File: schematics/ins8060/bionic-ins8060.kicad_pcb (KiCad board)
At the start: 2 copper layers, 25.4 x 68.6 mm, 8 parts, among them J1 Bionic-P135, J2 Bionic-P245, U1 INS8060, U2 11AA010-I/TT

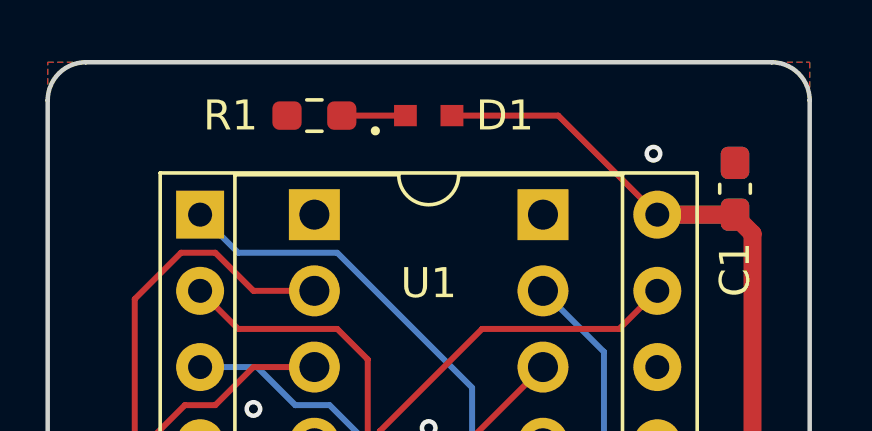
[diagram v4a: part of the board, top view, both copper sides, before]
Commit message: [schematics] Update LED footprint
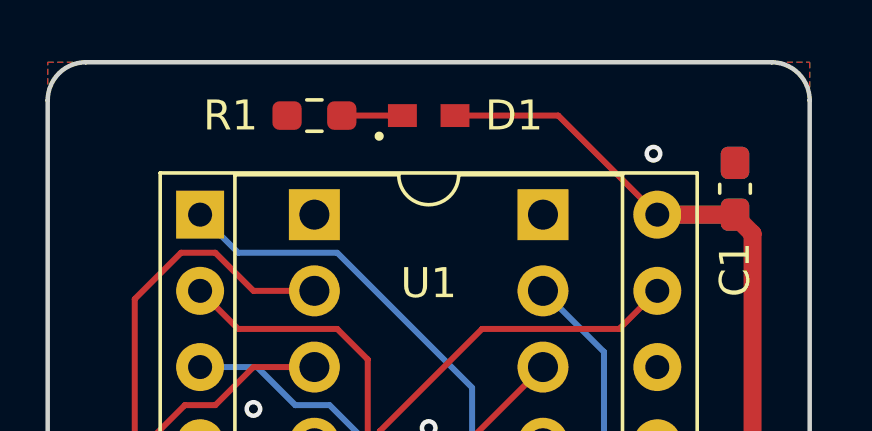
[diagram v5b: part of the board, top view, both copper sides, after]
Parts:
- D1: footprint 0-LocalLibrary:LED_CSL1901UW1_ROM -> 0-LocalLibrary:LED_CSL1901UW1_ROM-M

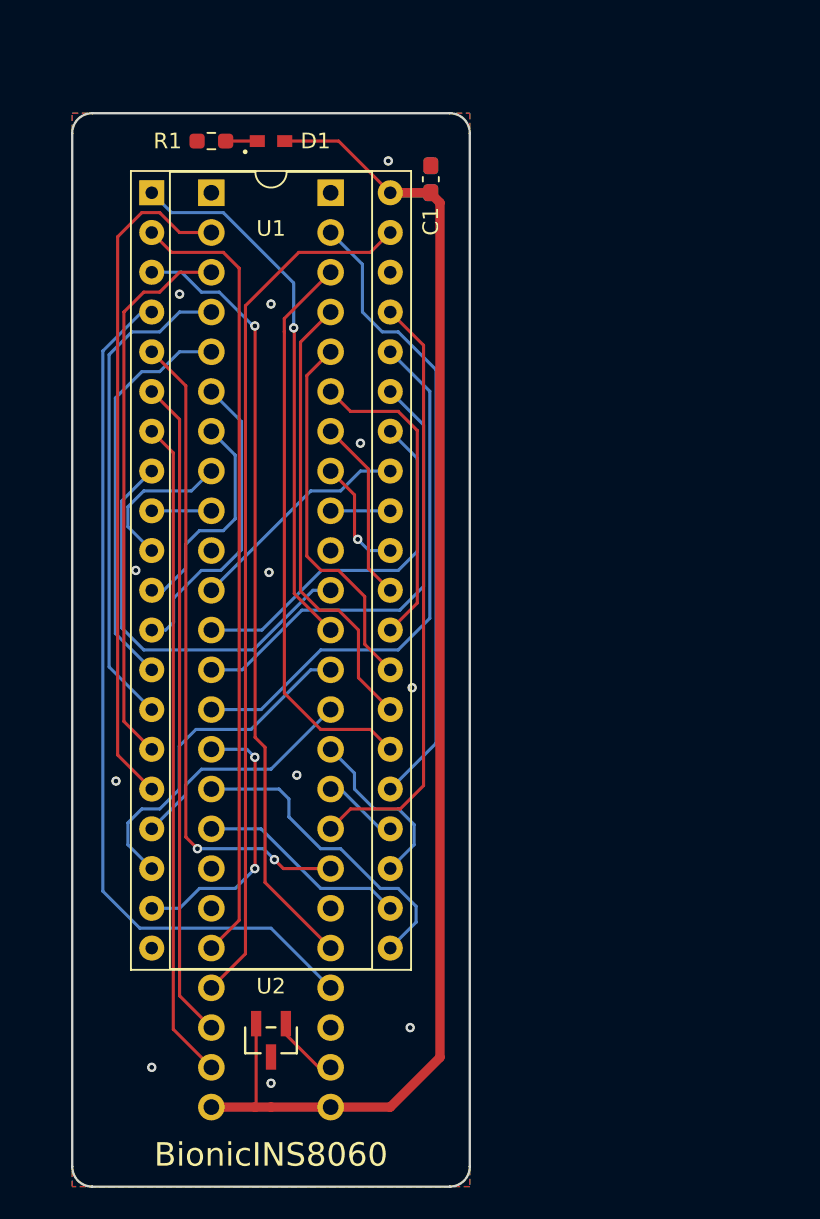
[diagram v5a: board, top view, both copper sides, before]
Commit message: [INS8060] Cleanup schematics
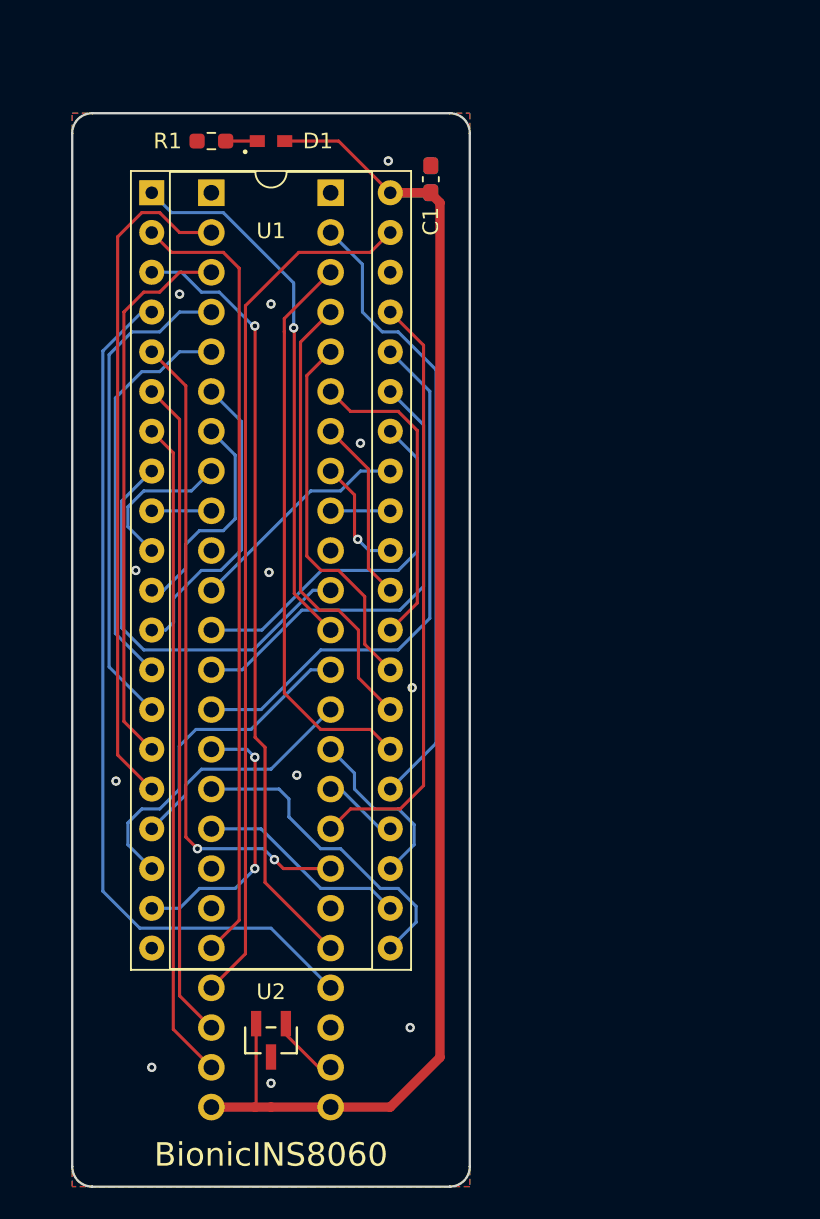
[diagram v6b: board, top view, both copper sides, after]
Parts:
- D1: footprint 0-LocalLibrary:LED_CSL1901UW1_ROM-M -> rhom:LED_CSL1901UW1_ROM-M
- J1: footprint 0-LocalLibrary:Bionic-P135_Vertical -> bionic:Bionic-P135_Vertical
- J2: footprint 0-LocalLibrary:Bionic-P245_Vertical -> bionic:Bionic-P245_Vertical
- U1: footprint 0-LocalLibrary:DIP-40_W15.24mm_Socket -> bionic:DIP-40_W15.24mm_Socket
- U2: footprint 0-LocalLibrary:SOT-23_MC_MCH-M -> microchip:SOT-23_MC_MCH-M
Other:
- rule pad_to_mask_clearance: 0.051 -> 0
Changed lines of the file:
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@@
 	)
 	(setup
-		(pad_to_mask_clearance 0.051)
-		(solder_mask_min_width 0.25)
+		(pad_to_mask_clearance 0)
 		(allow_soldermask_bridges_in_footprints no)
 		(aux_axis_origin 101 70)
@@
 	(net 47 "unconnected-(U1-XOUT-Pad38)")
 	(net 48 "Net-(D1-K)")
-	(footprint "0-LocalLibrary:LED_CSL1901UW1_ROM-M"
+	(footprint "rhom:LED_CSL1901UW1_ROM-M"
 		(layer "F.Cu")
 		(at 113.7 71.778)
@@
 		(tags "CSL1901UW1 ")
 		(property "Reference" "D1"
-			(at 2.8448 0 0)
+			(at 2.9972 0 0)
 			(unlocked yes)
 			(layer "F.SilkS")
@@
 			)
 		)
-		(property "Footprint" "0-LocalLibrary:LED_CSL1901UW1_ROM-M"
+		(property "Footprint" "rhom:LED_CSL1901UW1_ROM-M"
 			(at 0 0 0)
 			(layer "F.Fab")
@@
 			)
 		)
-		(property "Description" ""
+		(property "Description" "Red LED (Low Current Emission, SMD)"
 			(at 0 0 0)
 			(layer "F.Fab")
@@
 					(xy 113.3571 71.4224) (xy 114.0429 71.4224) (xy 114.0429 72.1336) (xy 113.3571 72.1336)
 				)
+			)
+		)
+		(model "${KIPRJMOD}/rhom.pretty/LED_CSL1901UW1_ROM.step"
+			(offset
+				(xyz 0 0 0)
+			)
+			(scale
+				(xyz 1 1 1)
+			)
+			(rotate
+				(xyz 0 0 0)
 			)
 		)
@@
 		)
 	)
-	(footprint "0-LocalLibrary:DIP-40_W15.24mm_Socket"
+	(footprint "bionic:DIP-40_W15.24mm_Socket"
 		(locked yes)
 		(layer "F.Cu")
@@
 		(tags "THT DIP DIL PDIP 2.54mm 15.24mm 600mil Socket")
 		(property "Reference" "U1"
-			(at 7.62 2.286 0)
+			(at 7.62 2.4384 0)
 			(layer "F.SilkS")
 			(effects
@@
 			)
 		)
-		(property "Footprint" "0-LocalLibrary:DIP-40_W15.24mm_Socket"
+		(property "Footprint" "bionic:DIP-40_W15.24mm_Socket"
 			(at 0 0 0)
 			(layer "F.Fab")
@@
 			)
 		)
-		(property "Description" ""
+		(property "Description" "8-bit General Purpose Microprocessor, DIP-40"
 			(at 0 0 0)
 			(layer "F.Fab")
@@
 		)
 	)
-	(footprint "0-LocalLibrary:SOT-23_MC_MCH-M"
+	(footprint "microchip:SOT-23_MC_MCH-M"
 		(layer "F.Cu")
 		(at 113.7 129.232 180)
 		(descr "Microchip 11AAxxx-I/TT UNI/O 1Kbit Serial EEPROM")
 		(property "Reference" "U2"
-			(at 0 3.4544 0)
+			(at 0 3.098 0)
 			(unlocked yes)
 			(layer "F.SilkS")
@@
 			)
 		)
-		(property "Footprint" "0-LocalLibrary:SOT-23_MC_MCH-M"
+		(property "Footprint" "microchip:SOT-23_MC_MCH-M"
 			(at 0 0 180)
 			(layer "F.Fab")
@@
 			)
 		)
-		(property "Description" ""
+		(property "Description" "UNI/O Serial EEPROM (1Kbit)"
 			(at 0 0 180)
 			(layer "F.Fab")
@@
 			(pintype "power_in")
 		)
-		(model "${KIPRJMOD}/0-LocalLibrary/SOT-23_MC_MCH.step"
+		(model "${KIPRJMOD}/microchip.pretty/SOT-23_MC_MCH.step"
 			(offset
 				(xyz 0 0 0)
@@
 		)
 	)
-	(footprint "0-LocalLibrary:Bionic-P245_Vertical"
+	(footprint "bionic:Bionic-P245_Vertical"
 		(locked yes)
 		(layer "B.Cu")
@@
 			)
 		)
-		(property "Footprint" "0-LocalLibrary:Bionic-P245_Vertical"
-			(at 0 0 180)
-			(layer "F.Fab")
+		(property "Footprint" "bionic:Bionic-P245_Vertical"
+			(at 0 0 0)
+			(layer "B.Fab")
 			(hide yes)
 			(effects
@@
 					(thickness 0.15)
 				)
+				(justify mirror)
 			)
 		)
 		(property "Datasheet" ""
-			(at 0 0 180)
-			(layer "F.Fab")
+			(at 0 0 0)
+			(layer "B.Fab")
 			(hide yes)
 			(effects
@@
 					(thickness 0.15)
 				)
-			)
-		)
-		(property "Description" ""
-			(at 0 0 180)
-			(layer "F.Fab")
+				(justify mirror)
+			)
+		)
+		(property "Description" "Generic connector, single row, 01x24, script generated (kicad-library-utils/schlib/autogen/connector/)"
+			(at 0 0 0)
+			(layer "B.Fab")
 			(hide yes)
 			(effects
@@
 					(thickness 0.15)
 				)
+				(justify mirror)
 			)
 		)
@@
 		)
 	)
-	(footprint "0-LocalLibrary:Bionic-P135_Vertical"
+	(footprint "bionic:Bionic-P135_Vertical"
 		(locked yes)
 		(layer "B.Cu")
@@
 			)
 		)
-		(property "Footprint" "0-LocalLibrary:Bionic-P135_Vertical"
-			(at 0 0 180)
-			(layer "F.Fab")
+		(property "Footprint" "bionic:Bionic-P135_Vertical"
+			(at 0 0 0)
+			(layer "B.Fab")
 			(hide yes)
 			(effects
@@
 					(thickness 0.15)
 				)
+				(justify mirror)
 			)
 		)
 		(property "Datasheet" ""
-			(at 0 0 180)
-			(layer "F.Fab")
+			(at 0 0 0)
+			(layer "B.Fab")
 			(hide yes)
 			(effects
@@
 					(thickness 0.15)
 				)
-			)
-		)
-		(property "Description" ""
-			(at 0 0 180)
-			(layer "F.Fab")
+				(justify mirror)
+			)
+		)
+		(property "Description" "Generic connector, single row, 01x24, script generated (kicad-library-utils/schlib/autogen/connector/)"
+			(at 0 0 0)
+			(layer "B.Fab")
 			(hide yes)
 			(effects
@@
 					(thickness 0.15)
 				)
-			)
-		)
+				(justify mirror)
+			)
+		)

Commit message: [INS8060] Update schematics
Remove unused pins from bionic connector
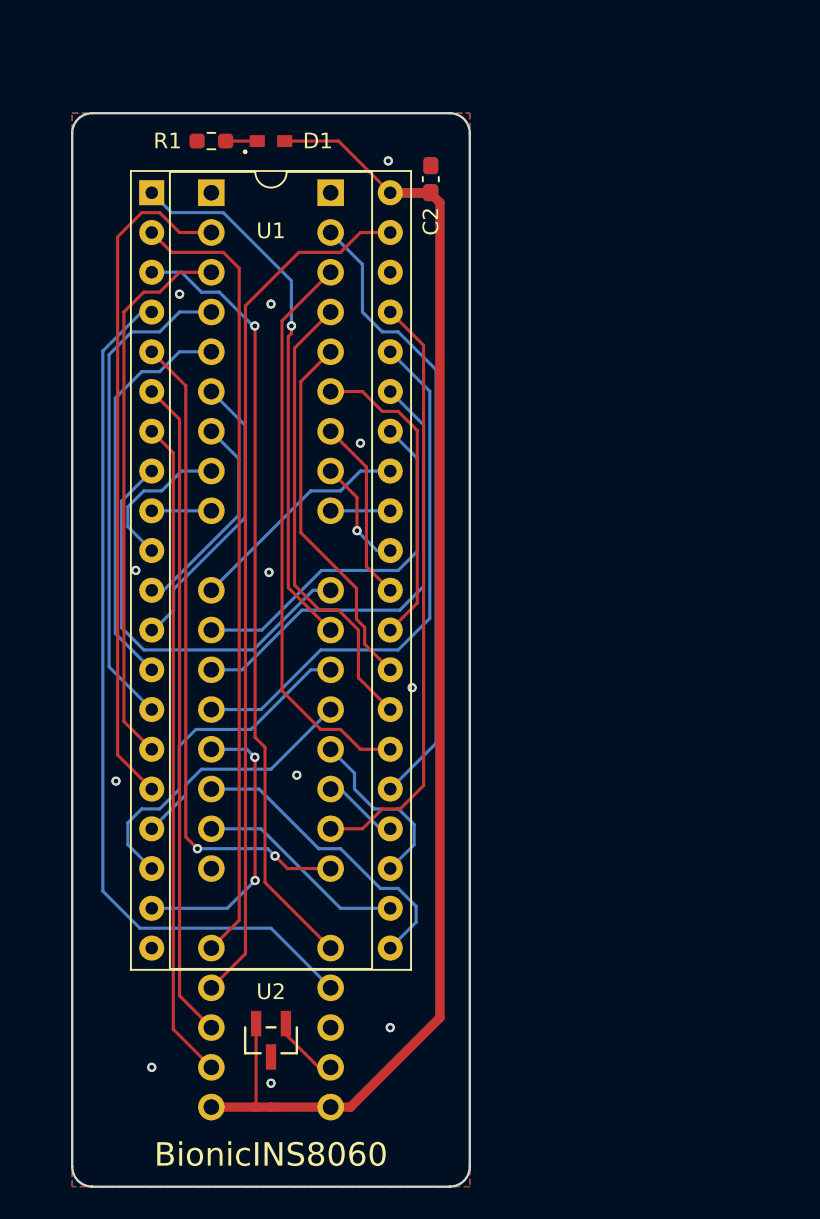
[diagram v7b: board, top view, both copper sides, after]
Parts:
- C1: moved to B.Cu
- C2: moved to F.Cu
- J1: footprint bionic:Bionic-P135_Vertical -> bionic:Bionic-P135_THT
- J2: footprint bionic:Bionic-P245_Vertical -> bionic:Bionic-P245_THT
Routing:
- net VCC: track 90.0 -> 88.5 mm
- net /P14: track 19.7 -> 18.7 mm
- net /P15: track 14.3 -> 13.6 mm
- net /P35: track 20.2 -> 19.5 mm
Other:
- board text added: "Rev. 7"
- board text removed: "Rev. 6"
